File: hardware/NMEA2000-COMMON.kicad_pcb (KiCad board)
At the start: 2 copper layers, 100 x 85 mm, 74 parts, among them J2 CAN, Q1 BSS138, Q2 BSS138, SW1 PRG, SW2 INSTANCE, SW3 BUS, U1 MCP2551-I-P, U101 74HC165, U2 TMR-2-2411, U3 74HCT595, U4 74HCT595, U5 Teensy_4.0

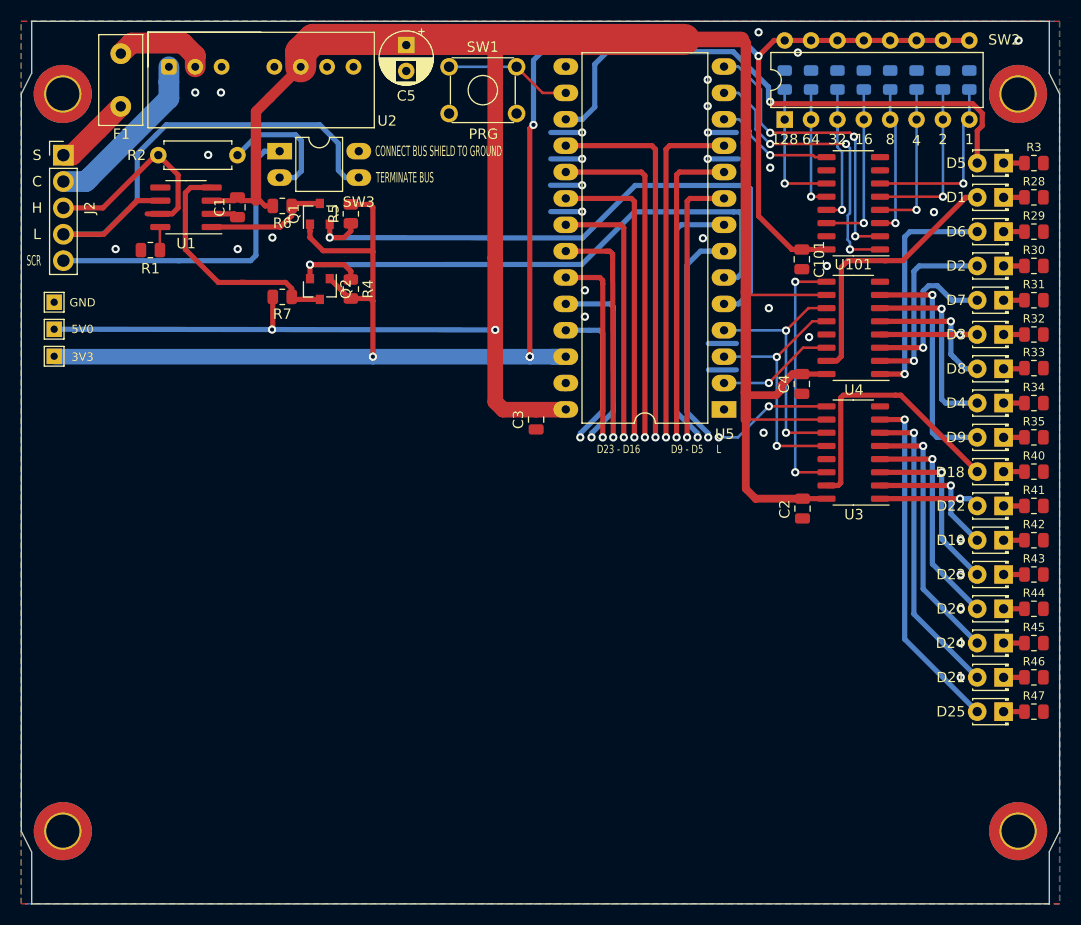
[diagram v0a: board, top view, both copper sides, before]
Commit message: Ground plane adjustments
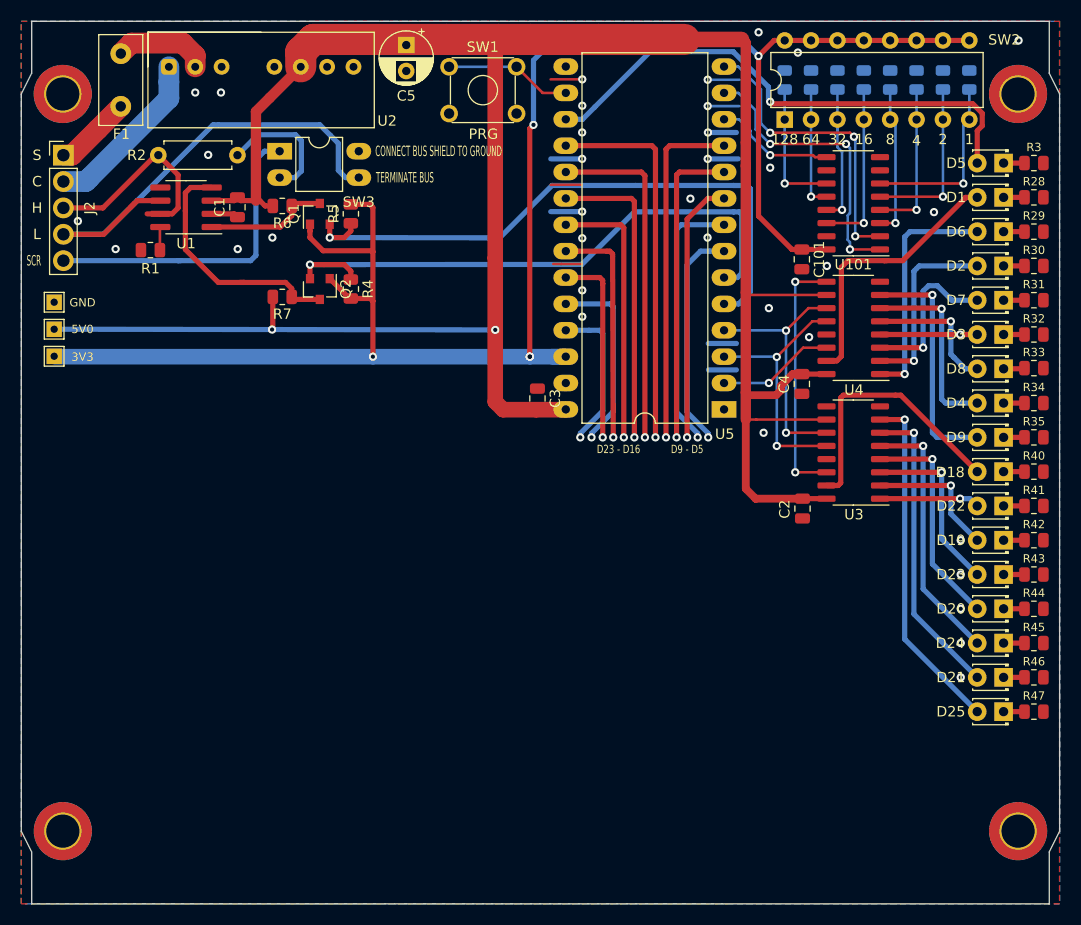
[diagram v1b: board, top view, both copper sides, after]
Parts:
- moved C3 2.04 mm to (69.7, 56.3), turned to 90 degrees
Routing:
- net Net-(U3-Pad9): track 11.6 -> 0.00 mm, vias 2 -> 0
- net GND: track 26.3 -> 35.3 mm, vias 31 -> 35
- net Net-(J2-Pad4): track 50.3 -> 47.7 mm
- net Net-(D5-Pad2): track 53.4 -> 51.0 mm
- net /D7: track 26.4 -> 25.4 mm

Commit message: Update NMEA2000-COMMON.kicad_pcb
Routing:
- net GND: track 35.3 -> 37.7 mm

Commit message: Tidy up
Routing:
- net /D23: track 14.6 -> 13.5 mm
- net /D5: track 21.5 -> 20.5 mm

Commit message: Relay
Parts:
- moved TEST 5V0 8.21 mm to (29.5, 47.1)
- moved TEST 5V0 4.11 mm to (26.3, 47.1)
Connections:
- net /INSTANCE_CP renamed /PISO_CP
- net /INSTANCE_PL renamed /PISO_PL
- net /INSTANCE_Q7 renamed /PISO_Q7
- net /LED_CLOCK renamed /SIPO_CLOCK
- net /LED_DATA renamed /SIPO_DATA
- net /LED_LATCH renamed /SIPO_LATCH
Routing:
- net +3V3: track 176.2 -> 164.9 mm, vias 5 -> 4
- net /CAN_RX: track 57.7 -> 53.8 mm
- net +5V: track 233.5 -> 234.6 mm, vias 2 -> 0
